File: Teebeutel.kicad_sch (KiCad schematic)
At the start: 166 parts, among them J1 RJ45_Shielded, J2 Battery, J3 Micro_SD_Card, J4 Conn_01x30_Female, J5 Conn_01x10_Female, J6 Conn_01x10_Female, M1 Motor_DC, Q1 S8050, Q2 S8050, Q3 AO3400, Q4 AO3400, Q5 AO3400, SW1 K1-1506SN-01, SW2 SW_SPST, U1 LIS2DE12, U10 SDB628, U11 TLV62568DBV, U12 SGP30, U13 PCA9539BS,118, U2 ESP32-WROOM-32, U3 SRV05-4, U4 TXB0104RUT, U5 MCP73831-2-OT, U6 PPSI262, U7 RM-V8xxC_TR1, U8 TLV70018_SOT23-5, U9 TXB0104RUT

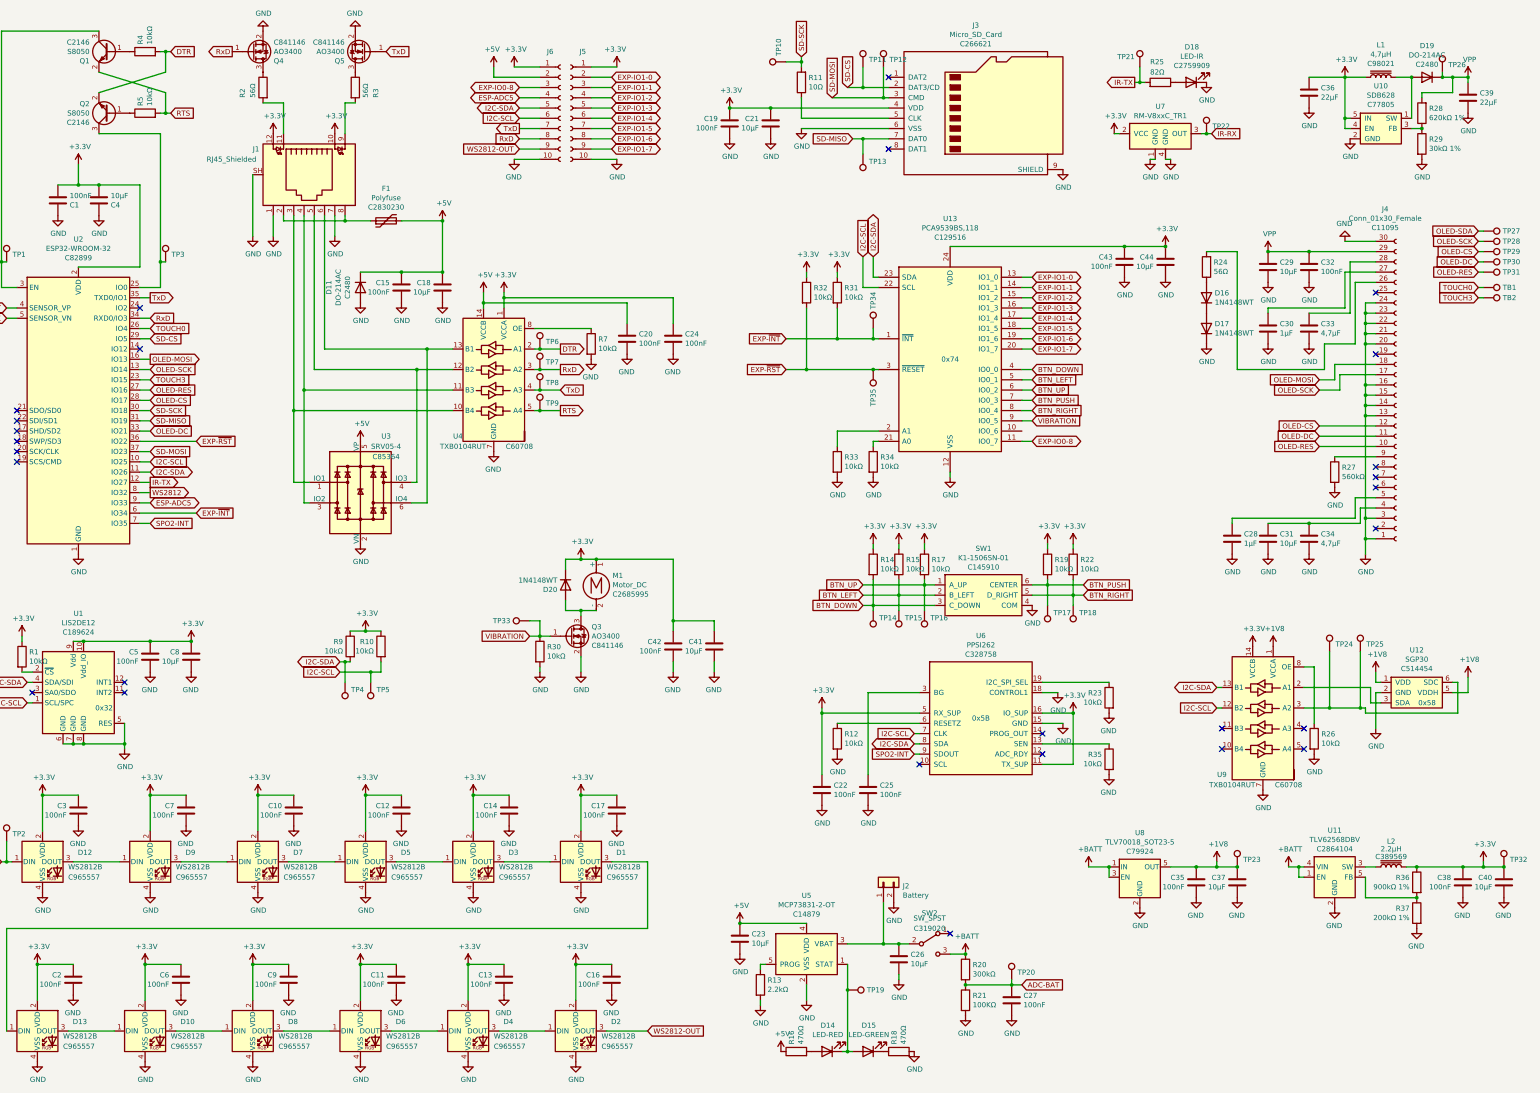
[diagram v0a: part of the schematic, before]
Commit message: pcb: finish routing
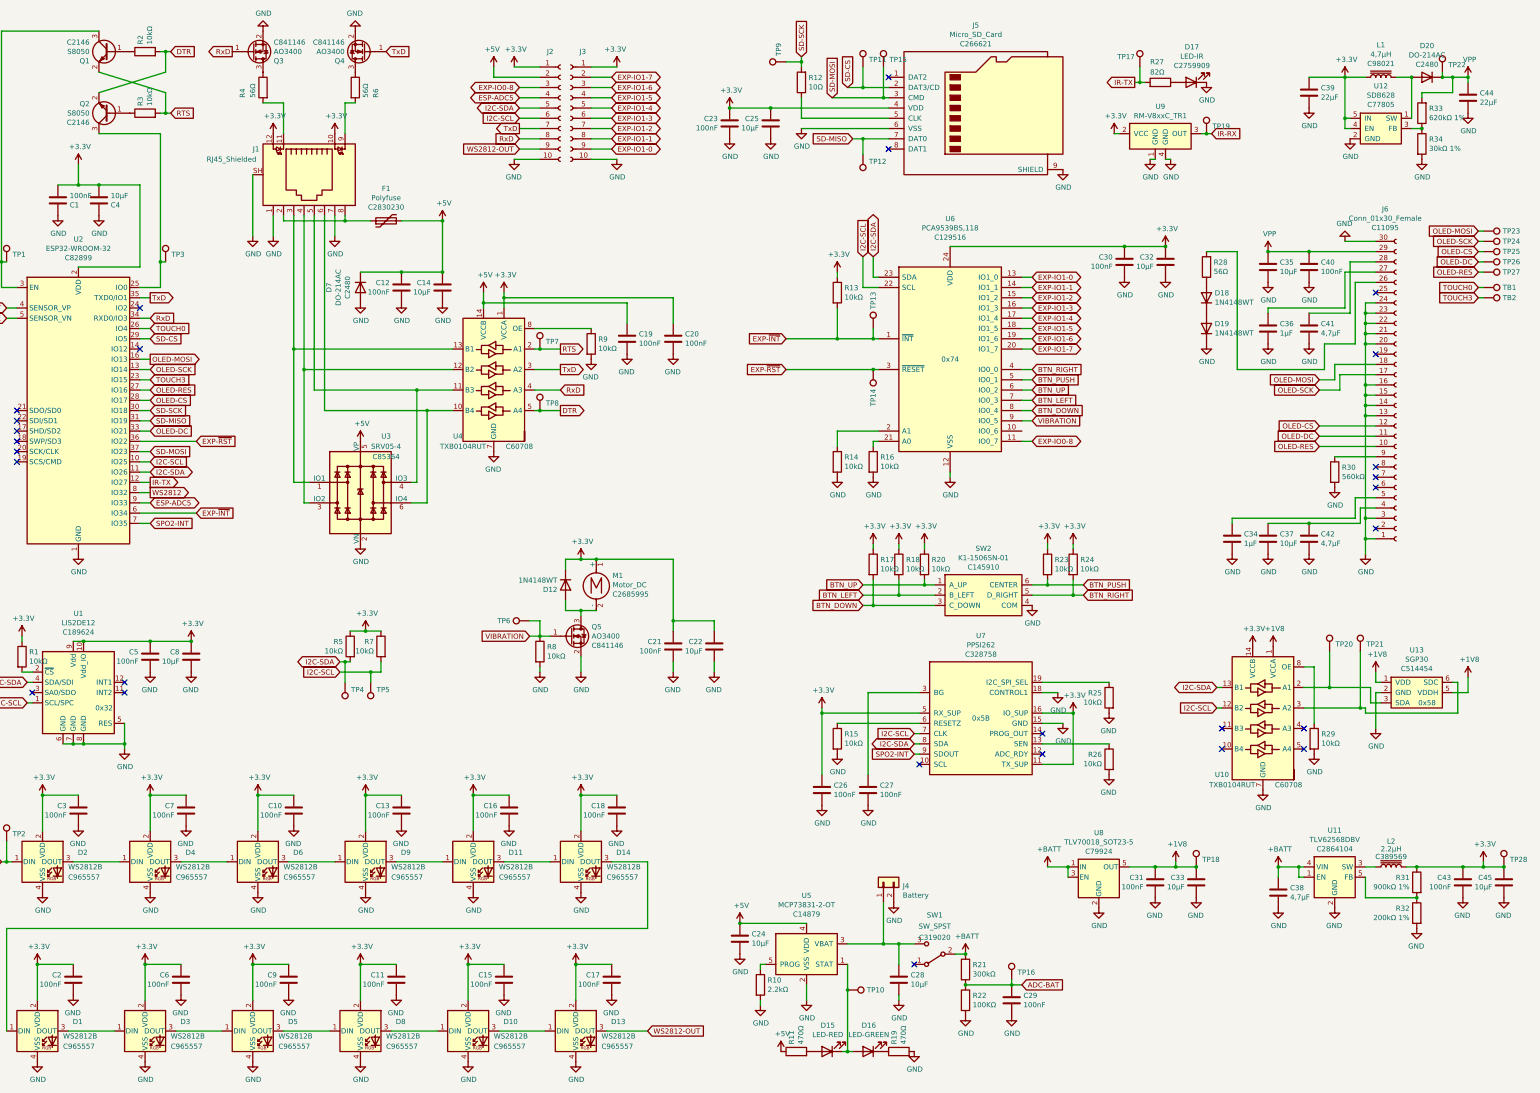
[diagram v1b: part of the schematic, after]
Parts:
- removed R32: 10kΩ, Resistor_SMD:R_0603_1608Metric, symbol Device:R
- removed TP14: Button Down, TestPoint:TestPoint_Pad_D1.0mm, symbol Connector:TestPoint
- removed TP15: Button Left, TestPoint:TestPoint_Pad_D1.0mm, symbol Connector:TestPoint
- removed TP16: Button Up, TestPoint:TestPoint_Pad_D1.0mm, symbol Connector:TestPoint
- removed TP17: Button Push, TestPoint:TestPoint_Pad_D1.0mm, symbol Connector:TestPoint
- removed TP18: Button Right, TestPoint:TestPoint_Pad_D1.0mm, symbol Connector:TestPoint
- removed TP7: TxD 3.3V, TestPoint:TestPoint_Pad_D1.0mm, symbol Connector:TestPoint
- removed TP8: RxD 3.3V, TestPoint:TestPoint_Pad_D1.0mm, symbol Connector:TestPoint
- added C38: 4,7µF, Capacitor_SMD:C_0603_1608Metric, symbol Device:C
- renumbered C15 to C12, C12 to C13, C18 to C14, C13 to C15, C14 to C16, C16 to C17, C17 to C18, C20 to C19, C24 to C20, C42 to C21, C41 to C22, C19 to C23, C23 to C24, C21 to C25, C22 to C26, C25 to C27, C26 to C28, C27 to C29, C43 to C30, C35 to C31, C44 to C32, C37 to C33, C28 to C34, C29 to C35, C30 to C36, C31 to C37, C36 to C39, C32 to C40, C33 to C41, C34 to C42, C38 to C43, C39 to C44, C40 to C45, D13 to D1, D4 to D10, D3 to D11, D20 to D12, D2 to D13, D1 to D14, D14 to D15, D15 to D16, D18 to D17, D16 to D18, D17 to D19, D12 to D2, D19 to D20, D10 to D3, D9 to D4, D8 to D5, D7 to D6, D11 to D7, D6 to D8, D5 to D9, J6 to J2, J5 to J3, J2 to J4, J3 to J5, J4 to J6, Q4 to Q3, Q5 to Q4, Q3 to Q5, R13 to R10, R16 to R11, R11 to R12, R31 to R13, R33 to R14, R12 to R15, R34 to R16, R14 to R17, R15 to R18, R18 to R19, R4 to R2, R17 to R20, R20 to R21, R21 to R22, R19 to R23, R22 to R24, R23 to R25, R35 to R26, R25 to R27, R24 to R28, R26 to R29, R5 to R3, R27 to R30, R36 to R31, R37 to R32, R28 to R33, R29 to R34, R2 to R4, R9 to R5, R3 to R6, R10 to R7, R30 to R8, R7 to R9, SW2 to SW1, SW1 to SW2, TP19 to TP10, TP13 to TP12, TP34 to TP13, TP35 to TP14, TP12 to TP15, TP20 to TP16, TP21 to TP17, TP23 to TP18, TP22 to TP19, TP24 to TP20, TP25 to TP21, TP26 to TP22, TP27 to TP23, TP28 to TP24, TP29 to TP25, TP30 to TP26, TP31 to TP27, TP32 to TP28, TP33 to TP6, TP6 to TP7, TP9 to TP8, TP10 to TP9, U9 to U10, U10 to U12, U12 to U13, U13 to U6, U6 to U7, U7 to U9
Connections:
- net OLED-SDA is gone; now on net OLED-MOSI: TP23.1
- net +BATT: now also SW1.2 (B), C38.1; no longer SW1.3 (C)
- net BTN_DOWN: now also U6.8 (IO0_4); no longer U6.4 (IO0_0)
- net BTN_LEFT: now also U6.7 (IO0_3); no longer U6.5 (IO0_1)
- net BTN_PUSH: now also U6.5 (IO0_1); no longer U6.7 (IO0_3)
- net BTN_RIGHT: now also U6.4 (IO0_0); no longer U6.8 (IO0_4)
- net DTR: now also TP8.1, U4.5 (A4); no longer TP7.1, U4.2 (A1)
- net EXP-IO1-0: now also J3.9 (Pin_9); no longer J3.2 (Pin_2)
- net EXP-IO1-1: now also J3.8 (Pin_8); no longer J3.3 (Pin_3)
- net EXP-IO1-2: now also J3.7 (Pin_7); no longer J3.4 (Pin_4)
- net EXP-IO1-3: now also J3.6 (Pin_6); no longer J3.5 (Pin_5)
- net EXP-IO1-4: now also J3.5 (Pin_5); no longer J3.6 (Pin_6)
- net EXP-IO1-5: now also J3.4 (Pin_4); no longer J3.7 (Pin_7)
- net EXP-IO1-6: now also J3.3 (Pin_3); no longer J3.8 (Pin_8)
- net EXP-IO1-7: now also J3.2 (Pin_2); no longer J3.9 (Pin_9)
- net GND: now also C38.2
- net RTS: now also TP7.1, U4.2 (A1); no longer TP8.1, U4.5 (A4)
- net RxD: now also U4.4 (A3); no longer U4.3 (A2)
- net TxD: now also U4.3 (A2); no longer U4.4 (A3)
- net at J1.3, U3.1 (IO1): now also U4.13 (B1); no longer U4.10 (B4)
- net at J1.4, U3.3 (IO2): now also U4.12 (B2); no longer U4.11 (B3)
- net at J1.5, U3.4 (IO3): now also U4.11 (B3); no longer U4.12 (B2)
- net at J1.6, U3.6 (IO4): now also U4.10 (B4); no longer U4.13 (B1)
- net at C28.1, J4.1 (Pin_1), U5.3 (VBAT): now also SW1.3 (C); no longer SW1.2 (B)
- net at U10.2 (A1), U13.3 (SDA): now also TP20.1
- net at TP21.1, U10.3 (A2), U13.6 (SDC): no longer TP20.1
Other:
- moved on the sheet: C28, C31, C33, SW1, TP18, U8

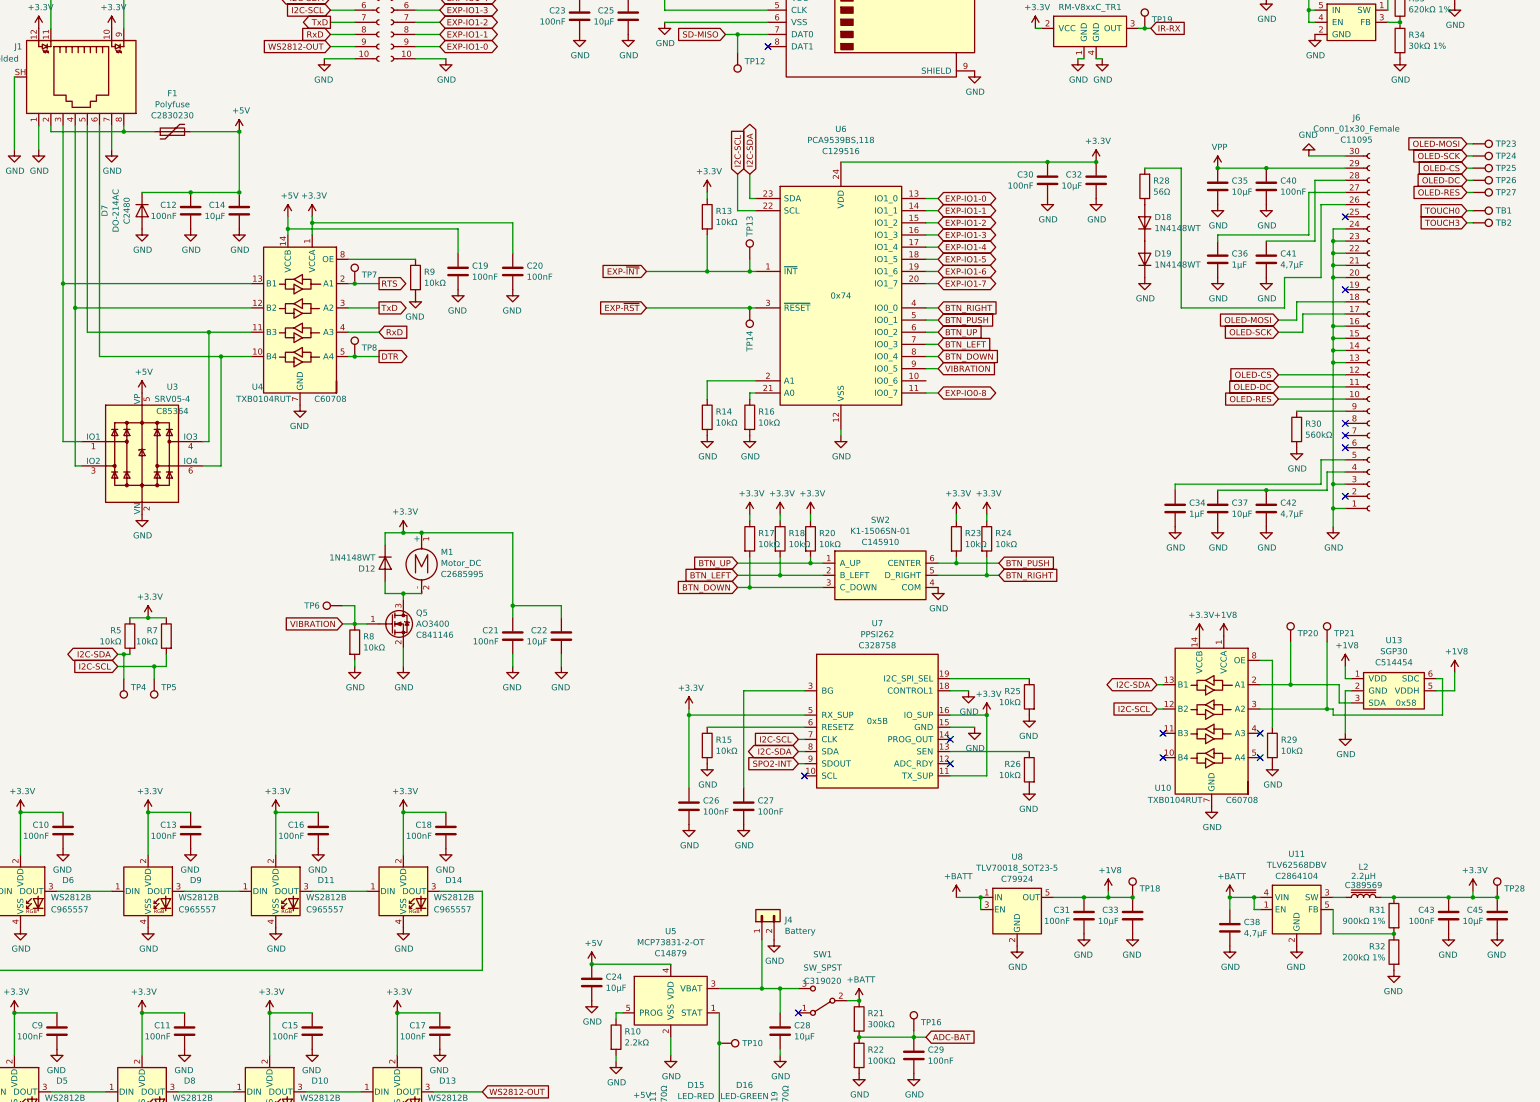
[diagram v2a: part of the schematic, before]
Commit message: Schematic: Lowered I2C pullup to 2.2k, exchanged I2C level shifter, changed FFC to mounting-pin version, fixed PPSI262 pinout
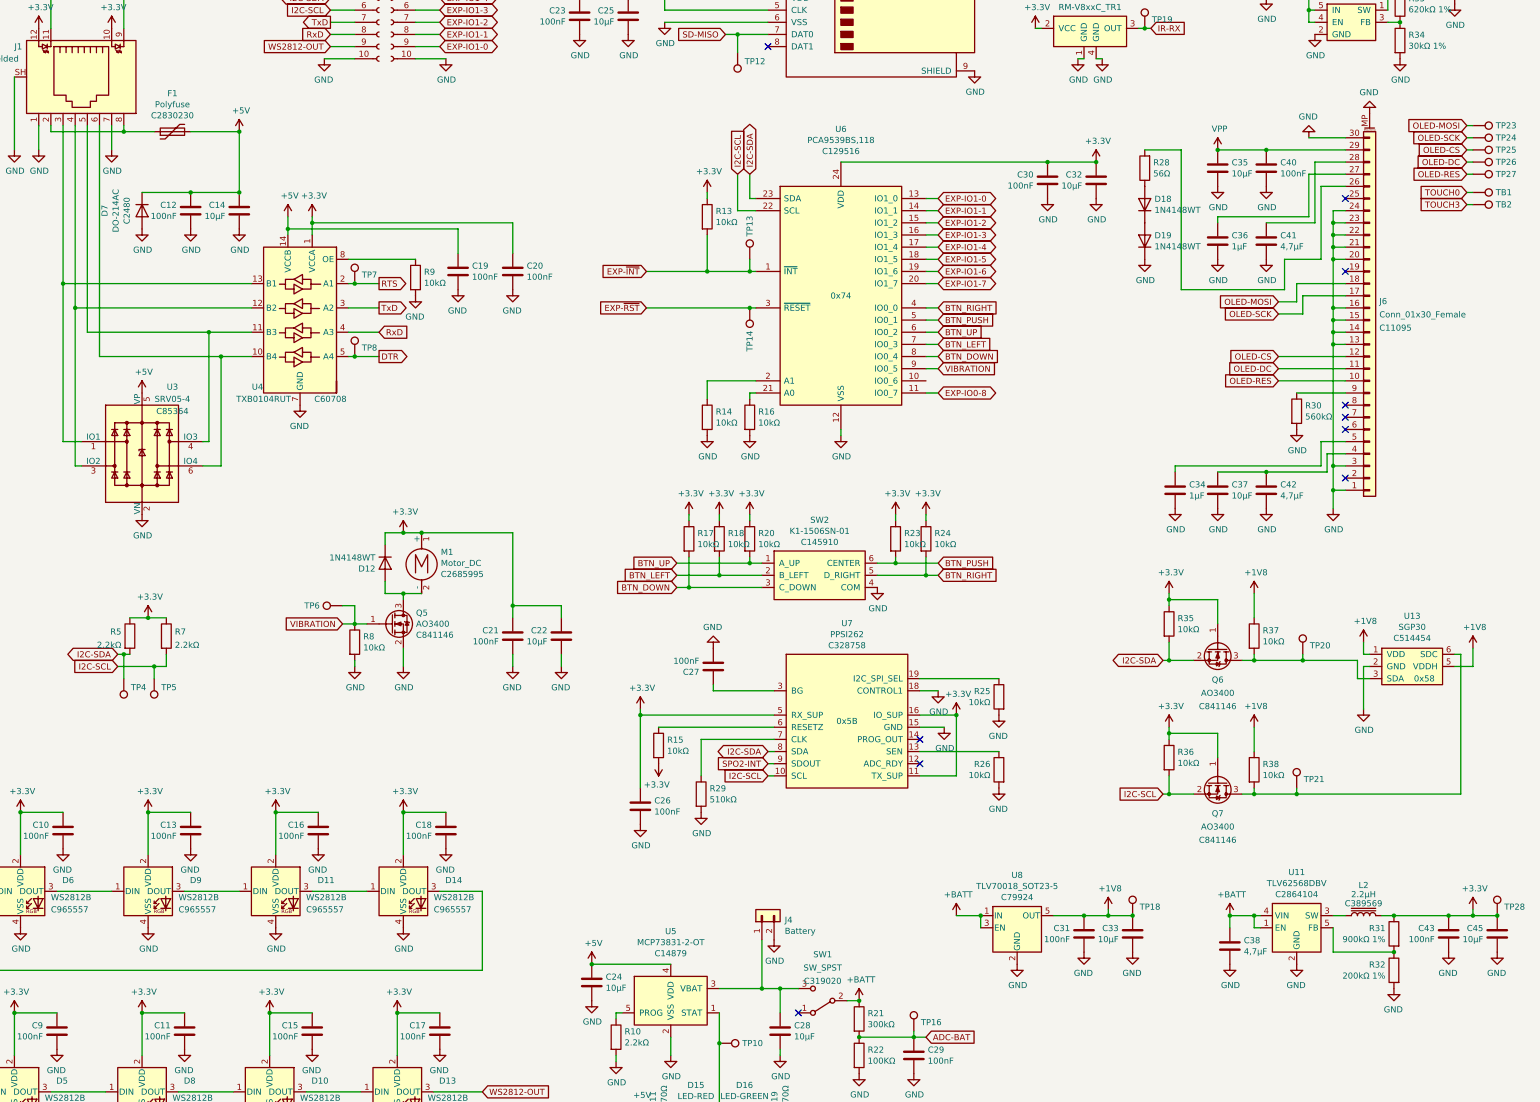
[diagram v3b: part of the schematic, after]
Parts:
- removed U10: TXB0104RUT, Package_SO:TSSOP-14_4.4x5mm_P0.65mm, symbol Logic_LevelTranslator:TXB0104PW
- added Q6, Q7: AO3400, Package_TO_SOT_SMD:SOT-23, symbol Transistor_FET:BSN20
- added R35, R36, R37, R38: 10kΩ, Resistor_SMD:R_0603_1608Metric, symbol Device:R
- J6: symbol Connector:Conn_01x30_Female -> Connector_Generic_MountingPin:Conn_01x30_MountingPin
- R29: value 10kΩ -> 510kΩ
- R5, R7: value 10kΩ -> 2.2kΩ; JLC 0603 -> R0603; LCSC C25804 -> C113303
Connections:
- net +1V8: now also R37.1, R38.1
- net +3V3: now also R15.2, Q6.1 (G), Q7.1 (G), R35.1, R36.1
- net GND: now also J6.MP (MountPin); no longer R15.2
- net I2C-SCL: now also U7.10 (SCL), Q7.2 (S), R36.2; no longer U7.7 (CLK)
- net I2C-SDA: now also Q6.2 (S), R35.2
- net at TP20.1, U13.3 (SDA): now also Q6.3 (D), R37.2
- net at TP21.1, U13.6 (SDC): now also Q7.3 (D), R38.2
- net at R29.1: now also U7.7 (CLK)
- no-connect marks 27 -> 22
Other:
- moved on the sheet: C26, C27, C31, C33, C34, C35, C36, C37, C38, C40, C41, C42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

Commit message: feat(): Connect ~RESET from PPSI to IO-Exp
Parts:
- removed R15: 10kΩ, Resistor_SMD:R_0603_1608Metric, symbol Device:R
- renumbered C39 to C1, C32 to C10, C12 to C11, C14 to C12, C36 to C13, C41 to C14, C19 to C15, C20 to C16, C34 to C17, C37 to C18, C42 to C19, C44 to C2, C21 to C20, C22 to C21, C5 to C22, C8 to C23, C27 to C24, C26 to C25, C3 to C26, C7 to C27, C10 to C28, C13 to C29, C23 to C3, C16 to C30, C18 to C31, C31 to C32, C43 to C34, C45 to C35, C38 to C36, C24 to C37, C2 to C38, C6 to C39, C25 to C4, C9 to C40, C11 to C41, C15 to C42, C17 to C43, C28 to C44, C29 to C45, C1 to C5, C4 to C6, C35 to C7, C40 to C8, C30 to C9, D20 to D1, D9 to D10, D14 to D12, D1 to D13, D3 to D14, D5 to D15, D8 to D16, D10 to D17, D13 to D18, D15 to D19, D17 to D2, D16 to D20, D18 to D3, D7 to D4, D19 to D5, D12 to D6, D2 to D7, D4 to D8, D6 to D9, J2 to J1, J3 to J2, J5 to J3, J1 to J4, J6 to J5, J4 to J6, Q3 to Q2, Q4 to Q3, Q2 to Q4, R2 to R1, R13 to R10, R9 to R11, R30 to R12, R14 to R13, R16 to R14, R17 to R15, R18 to R16, R20 to R17, R23 to R18, R24 to R19, R12 to R2, R35 to R20, R5 to R21, R7 to R22, R37 to R23, R8 to R24, R1 to R25, R25 to R26, R36 to R27, R26 to R28, R38 to R29, R27 to R3, R29 to R30, R21 to R33, R10 to R34, R22 to R35, R11 to R36, R19 to R37, R6 to R5, R3 to R6, R33 to R7, R34 to R8, R28 to R9, SW2 to SW1, SW1 to SW2, TP9 to TP1, TP25 to TP10, TP26 to TP11, TP27 to TP12, TP1 to TP13, TP3 to TP14, TP13 to TP15, TP7 to TP16, TP14 to TP17, TP8 to TP18, TP6 to TP19, TP11 to TP2, TP4 to TP21, TP5 to TP22, TP21 to TP23, TP2 to TP24, TP18 to TP25, TP28 to TP26, TP16 to TP27, TP10 to TP28, TP15 to TP3, TP17 to TP4, TP22 to TP5, TP19 to TP6, TP12 to TP7, TP23 to TP8, TP24 to TP9, U12 to U1, U8 to U10, U5 to U12, U9 to U2, U6 to U3, U2 to U5, U3 to U6, U13 to U7, U7 to U8, U1 to U9
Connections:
- net SPO2-~{RESET}: now reaches U8.6 (RESETZ)
- net SPO2-~{RESET}: now also U3.10 (IO0_6)

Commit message: chore: update docs
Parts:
- R30: LCSC C25804 -> (none)
- TP8: value OLED SDA -> OLED MOSI
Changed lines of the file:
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@@
       (effects (font (size 1.27 1.27)) (justify left))
     )
-    (property "Value" "OLED SDA" (id 1) (at 395.6558 66.2432 0)
+    (property "Value" "OLED MOSI" (id 1) (at 395.6558 66.2432 0)
       (effects (font (size 1.27 1.27)) (justify left) hide)
     )
@@
       (effects (font (size 1.27 1.27)) hide)
     )
-    (property "LCSC" "C25804" (id 5) (at 233.68 204.47 0)
+    (property "LCSC" "" (id 5) (at 233.68 204.47 0)
       (effects (font (size 1.27 1.27)) hide)
     )
@@
     )
     (path "/00000000-0000-0000-0000-000061a9f0c1"
-      (reference "TP8") (unit 1) (value "OLED SDA") (footprint "TestPoint:TestPoint_Pad_D1.0mm")
+      (reference "TP8") (unit 1) (value "OLED MOSI") (footprint "TestPoint:TestPoint_Pad_D1.0mm")
     )
     (path "/00000000-0000-0000-0000-000061aa00ca"
